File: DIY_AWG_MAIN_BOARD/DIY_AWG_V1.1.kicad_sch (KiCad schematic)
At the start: 4 parts

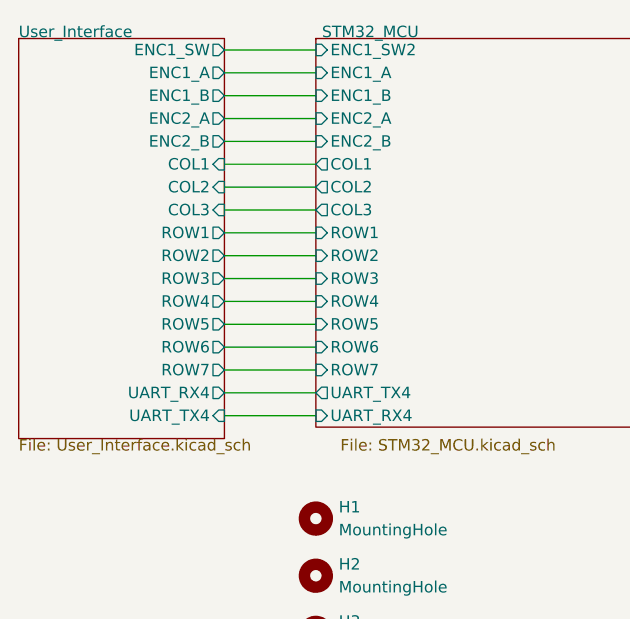
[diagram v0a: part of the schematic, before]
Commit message: Updated daughter board and main board PCB design schematics
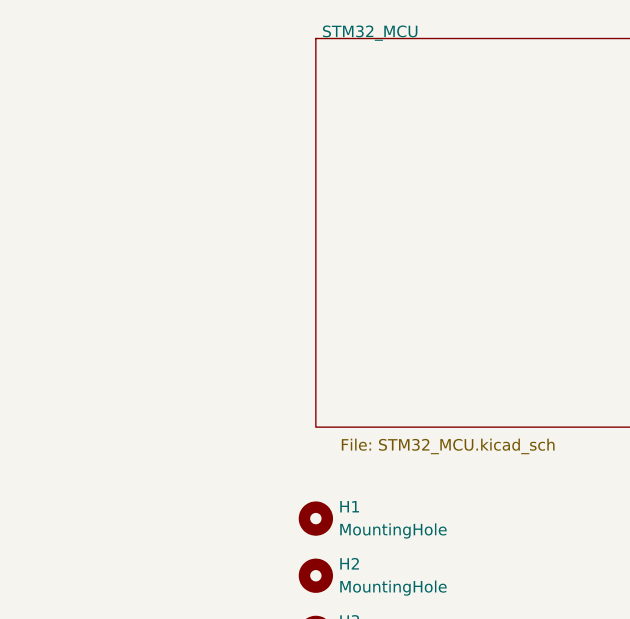
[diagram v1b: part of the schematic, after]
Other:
- removed sheet User_Interface
- sheet STM32_MCU ports: added none; removed COL1, COL2, COL3, ENC1_A, ENC1_B, ENC1_SW2, ENC2_A, ENC2_B, ROW1, ROW2, ROW3, ROW4, ROW5, ROW6, ROW7, UART_RX4, UART_TX4

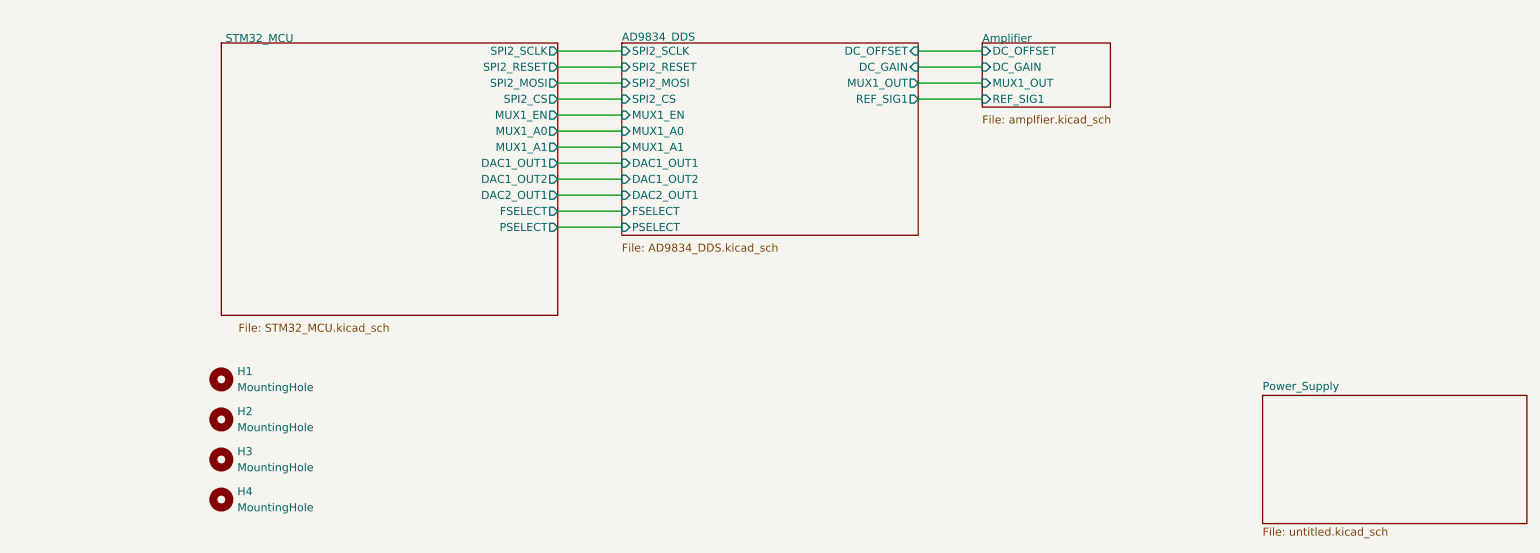
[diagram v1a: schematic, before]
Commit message: Updated main board schematic and PCB
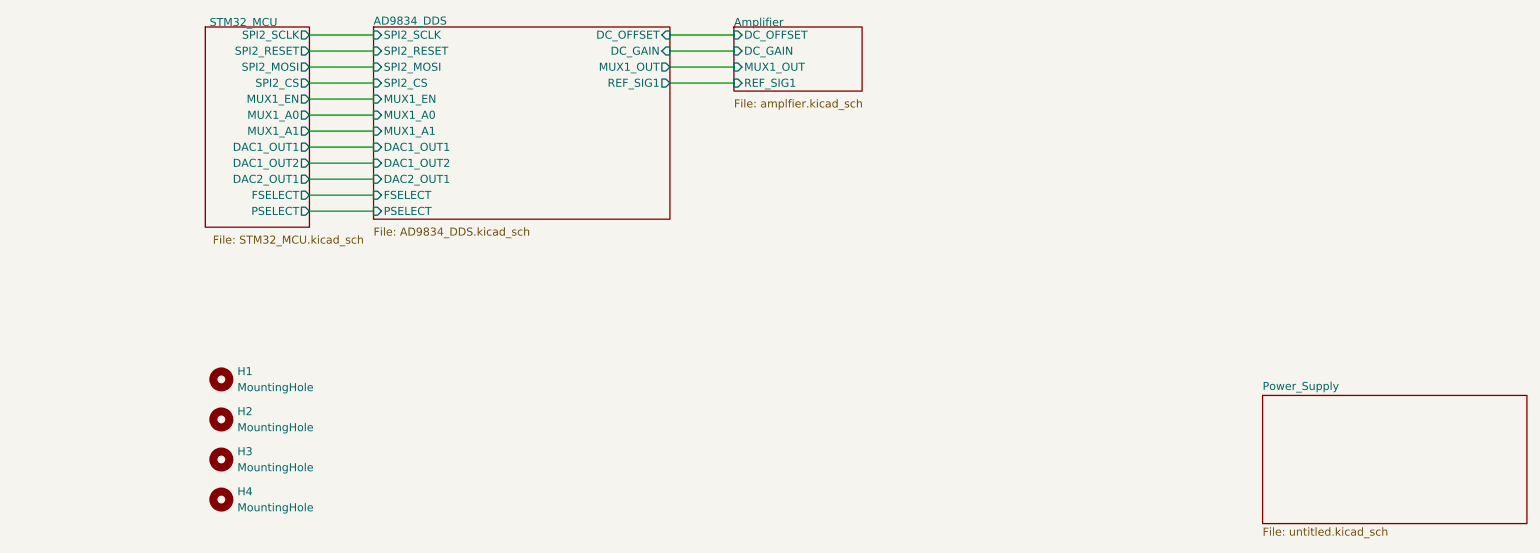
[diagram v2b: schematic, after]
